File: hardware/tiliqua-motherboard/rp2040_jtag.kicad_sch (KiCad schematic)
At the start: 31 parts, among them J5 USB_C_Receptacle_USB2.0_14P, SW2 SW_Tactile_SPST, U12 W25Q128JVP, U2 RP2040(QFN-56_7x7mm_P0.4mm), Y1 Crystal_GND24_Small

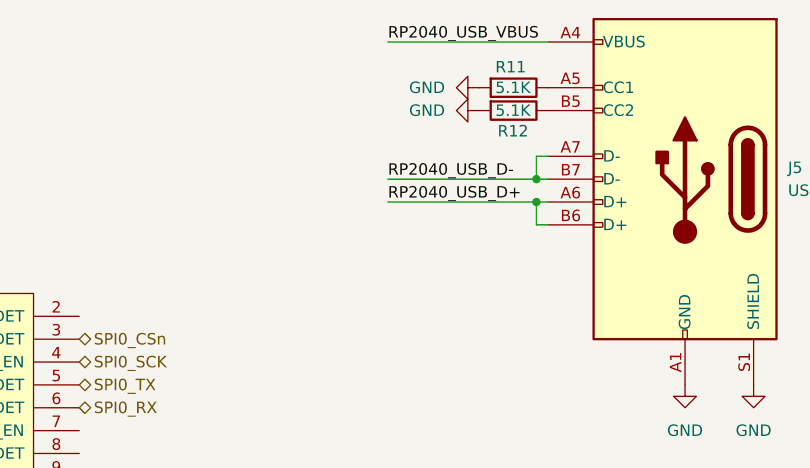
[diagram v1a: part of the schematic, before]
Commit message: * USB1/USB2 ESD protection
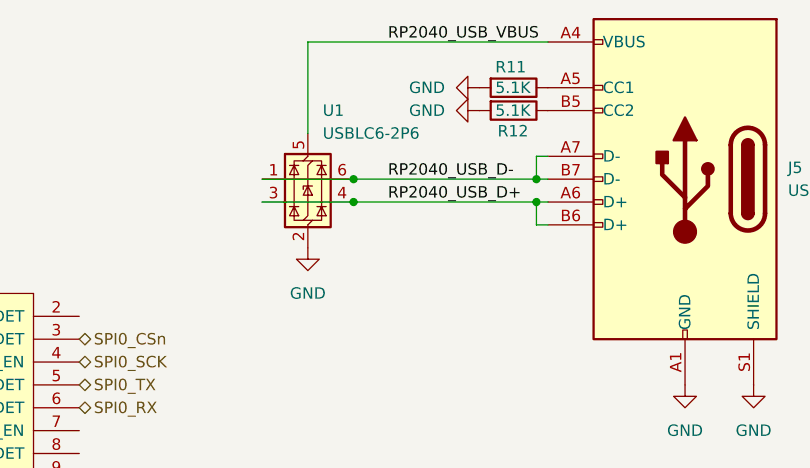
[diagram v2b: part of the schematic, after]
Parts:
- added U1: USBLC6-2P6, Package_TO_SOT_SMD:SOT-666, symbol Power_Protection:USBLC6-2P6
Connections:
- net GND: now also U1.2 (GND)
- net RP2040_USB_D+: now also U1.3 (I/O2), U1.4 (I/O2)
- net RP2040_USB_D-: now also U1.1 (I/O1), U1.6 (I/O1)
- net RP2040_USB_VBUS: now also U1.5 (VBUS)
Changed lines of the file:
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@@
 	)
 	(junction
+		(at 232.41 38.1)
+		(diameter 0)
+		(color 0 0 0 0)
+	)
+	(junction
 		(at 69.85 73.66)
 		(diameter 0)
@@
 	)
 	(junction
+		(at 232.41 40.64)
+		(diameter 0)
+		(color 0 0 0 0)
+	)
+	(junction
 		(at 92.71 99.06)
 		(diameter 0)
@@
 	(wire
 		(pts
+			(xy 227.33 22.86) (xy 227.33 33.02)
+		)
+		(stroke
+			(width 0)
+			(type default)
+		)
+	)
+	(wire
+		(pts
 			(xy 59.69 43.18) (xy 59.69 53.34)
 		)
@@
 	(wire
 		(pts
+			(xy 222.25 38.1) (xy 232.41 38.1)
+		)
+		(stroke
+			(width 0)
+			(type default)
+		)
+	)
+	(wire
+		(pts
 			(xy 69.85 73.66) (xy 72.39 73.66)
 		)
@@
 	(wire
 		(pts
+			(xy 227.33 22.86) (xy 254 22.86)
+		)
+		(stroke
+			(width 0)
+			(type default)
+		)
+	)
+	(wire
+		(pts
 			(xy 90.17 43.18) (xy 90.17 76.2)
 		)
@@
 	(wire
 		(pts
-			(xy 254 43.18) (xy 252.73 43.18)
+			(xy 232.41 38.1) (xy 252.73 38.1)
 		)
 		(stroke
@@
 	(wire
 		(pts
-			(xy 59.69 76.2) (xy 59.69 88.9)
+			(xy 254 43.18) (xy 252.73 43.18)
 		)
 		(stroke
@@
 	(wire
 		(pts
-			(xy 62.23 91.44) (xy 59.69 91.44)
+			(xy 59.69 76.2) (xy 59.69 88.9)
 		)
 		(stroke
@@
 	(wire
 		(pts
-			(xy 88.9 55.88) (xy 88.9 52.07)
+			(xy 62.23 91.44) (xy 59.69 91.44)
 		)
 		(stroke
@@
 	(wire
 		(pts
-			(xy 59.69 30.48) (xy 59.69 33.02)
+			(xy 88.9 55.88) (xy 88.9 52.07)
 		)
 		(stroke
@@
 	(wire
 		(pts
-			(xy 92.71 88.9) (xy 92.71 91.44)
+			(xy 59.69 30.48) (xy 59.69 33.02)
 		)
 		(stroke
@@
 	(wire
 		(pts
-			(xy 236.22 22.86) (xy 254 22.86)
+			(xy 92.71 88.9) (xy 92.71 91.44)
 		)
 		(stroke
@@
 	(wire
 		(pts
+			(xy 222.25 40.64) (xy 232.41 40.64)
+		)
+		(stroke
+			(width 0)
+			(type default)
+		)
+	)
+	(wire
+		(pts
 			(xy 90.17 76.2) (xy 95.25 76.2)
 		)
@@
 	(wire
 		(pts
+			(xy 232.41 40.64) (xy 252.73 40.64)
+		)
+		(stroke
+			(width 0)
+			(type default)
+		)
+	)
+	(wire
+		(pts
 			(xy 59.69 119.38) (xy 59.69 124.46)
 		)
@@
 	(wire
 		(pts
-			(xy 236.22 40.64) (xy 252.73 40.64)
-		)
-		(stroke
-			(width 0)
-			(type default)
-		)
-	)
-	(wire
-		(pts
 			(xy 252.73 43.18) (xy 252.73 40.64)
 		)
@@
 	(wire
 		(pts
-			(xy 236.22 38.1) (xy 252.73 38.1)
-		)
-		(stroke
-			(width 0)
-			(type default)
-		)
-	)
-	(wire
-		(pts
 			(xy 59.69 93.98) (xy 59.69 96.52)
 		)
@@
 					(unit 1)
 				)
+			)
+		)
+	)
+	(symbol
+		(lib_id "power:GND")
+		(at 227.33 45.72 0)
+		(mirror y)
+		(unit 1)
+		(exclude_from_sim no)
+		(in_bom yes)
+		(on_board yes)
+		(dnp no)
+		(fields_autoplaced yes)
+		(property "Reference" "#PWR07"
+			(at 227.33 52.07 0)
+			(effects
+				(font
+					(size 1.27 1.27)
+				)
+				(hide yes)
+			)
+		)
+		(property "Value" "GND"
+			(at 227.33 50.8 0)
+			(effects
+				(font
+					(size 1.27 1.27)
+				)
+			)
+		)
+		(property "Footprint" ""
+			(at 227.33 45.72 0)
+			(effects
+				(font
+					(size 1.27 1.27)
+				)
+				(hide yes)
+			)
+		)
+		(property "Datasheet" ""
+			(at 227.33 45.72 0)
+			(effects
+				(font
+					(size 1.27 1.27)
+				)
+				(hide yes)
+			)
+		)
+		(property "Description" ""
+			(at 227.33 45.72 0)
+			(effects
+				(font
+					(size 1.27 1.27)
+				)
+				(hide yes)
+			)
+		)
+		(pin "1"
+		)
+		(instances
+			(project "tiliqua-motherboard"
+				(path "/df6062c3-a570-4505-924c-c7fe32df3670/32fbecb8-cfc0-4e90-9d95-f47a131c8376"
+					(reference "#PWR07")
+					(unit 1)
+				)
+			)
+		)
+	)
+	(symbol
+		(lib_id "Power_Protection:USBLC6-2P6")
+		(at 227.33 38.1 0)
+		(unit 1)
+		(exclude_from_sim no)
+		(in_bom yes)
+		(on_board yes)
+		(dnp no)
+		(fields_autoplaced yes)
+		(property "Reference" "U1"
+			(at 228.9811 30.48 0)
+			(effects
+				(font
+					(size 1.27 1.27)
+				)
+				(justify left)
+			)
+		)
+		(property "Value" "USBLC6-2P6"
+			(at 228.9811 33.02 0)
+			(effects
+				(font
+					(size 1.27 1.27)
+				)
+				(justify left)
+			)
+		)
+		(property "Footprint" "Package_TO_SOT_SMD:SOT-666"
+			(at 228.346 44.831 0)
+			(effects
+				(font
+					(size 1.27 1.27)
+					(italic yes)
+				)
+				(justify left)
+				(hide yes)
+			)
+		)
+		(property "Datasheet" "https://www.st.com/resource/en/datasheet/usblc6-2.pdf"
+			(at 228.346 46.736 0)
+			(effects
+				(font
+					(size 1.27 1.27)
+				)
+				(justify left)
+				(hide yes)
+			)
+		)
+		(property "Description" "Very low capacitance ESD protection diode, 2 data-line, SOT-666"
+			(at 227.33 38.1 0)
+			(effects
+				(font
+					(size 1.27 1.27)
+				)
+				(hide yes)
+			)
+		)
+		(pin "1"
+		)
+		(pin "4"
+		)
+		(pin "6"
+		)
+		(pin "2"
+		)
+		(pin "5"
+		)
+		(pin "3"
+		)
+		(instances
+			(project ""
+				(path "/df6062c3-a570-4505-924c-c7fe32df3670/32fbecb8-cfc0-4e90-9d95-f47a131c8376"
+					(reference "U1")
+					(unit 1)
+				)

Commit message: * BOM: update some LCSC fields
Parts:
- U1: LCSC (none) -> C15999
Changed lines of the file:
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@@
+			)
+		)
+		(property "LCSC" "C15999"
+			(at 227.33 38.1 0)
+			(effects
+				(font
+					(size 1.27 1.27)
+				)
+				(hide yes)
 			)
 		)
